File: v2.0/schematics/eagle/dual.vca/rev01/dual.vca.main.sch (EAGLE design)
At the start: 50 parts, among them IC1 TL084P, IC2 TL082P, IC3 LM324N, T1 BC547, T2 BC547, T3 BC547

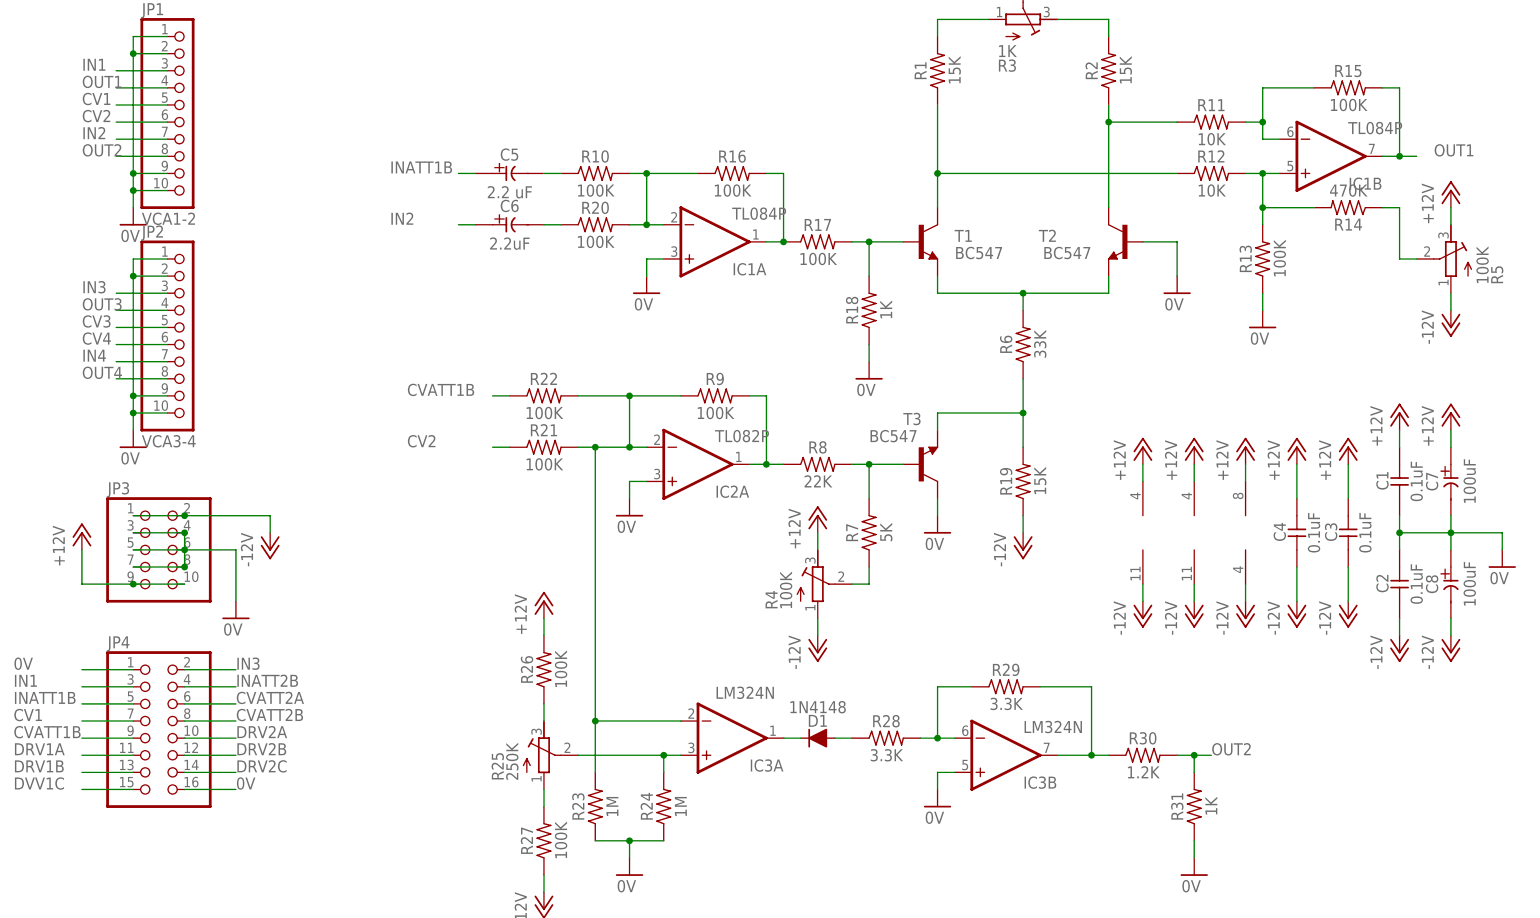
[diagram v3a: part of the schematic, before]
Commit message: Add DRV to dual.vca schem
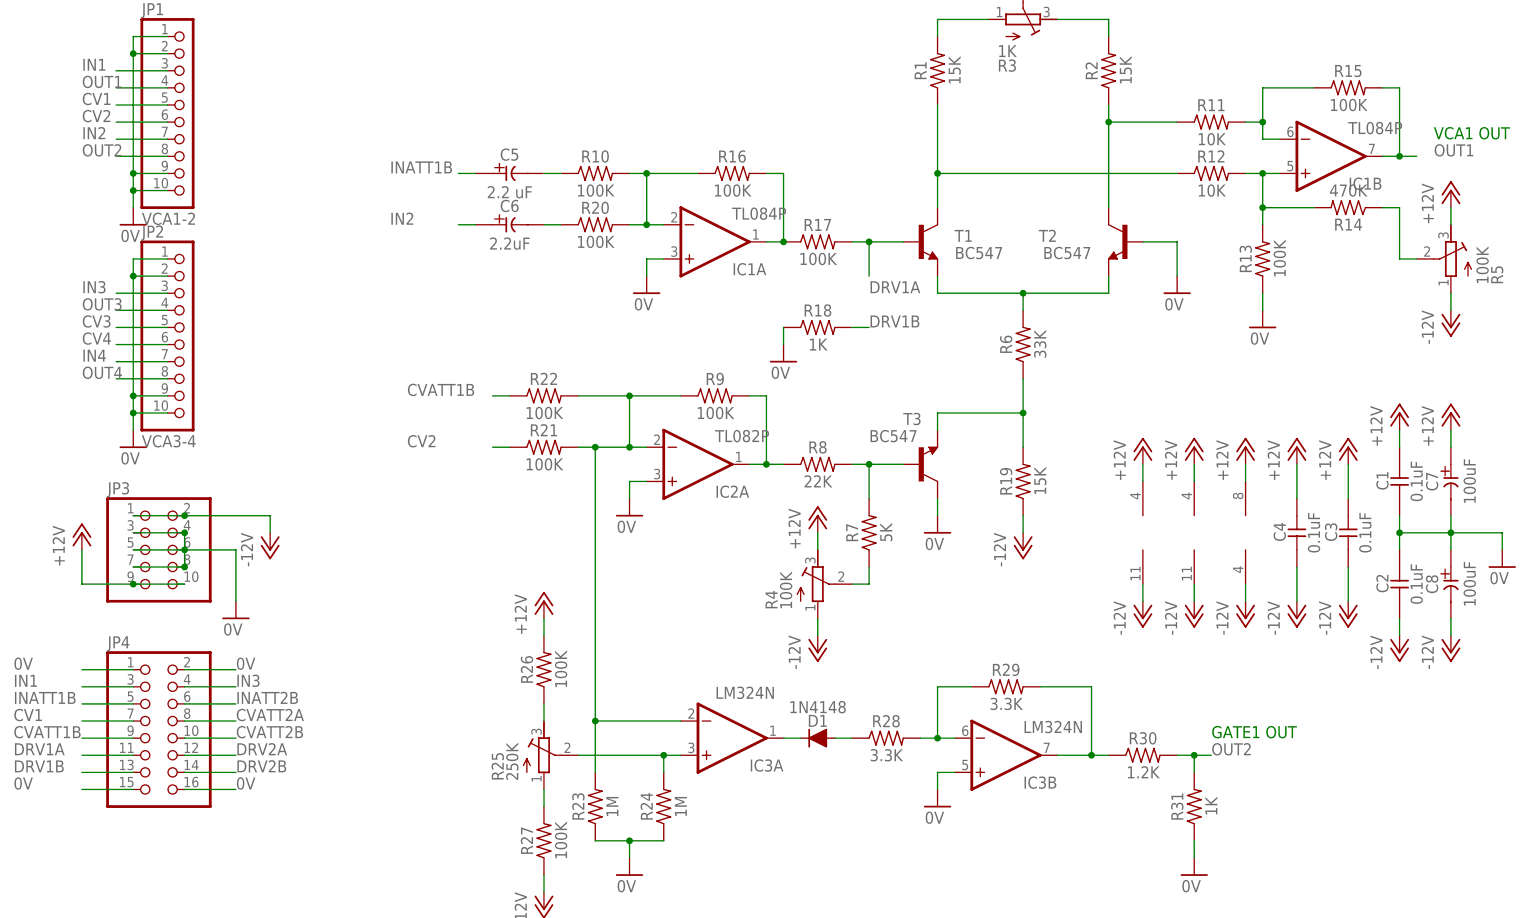
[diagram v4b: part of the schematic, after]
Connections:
- removed net DRV2C: JP4.14
- removed net DVV1C: JP4.15
- removed net N$4: R17.2, R18.2, T1.B
- net 0V: now also JP4.15, JP4.2
- net CVATT2A: now also JP4.8; no longer JP4.6
- net CVATT2B: now also JP4.10; no longer JP4.8
- net DRV1A: now also R17.2, T1.B
- net DRV1B: now also R18.2
- net DRV2A: now also JP4.12; no longer JP4.10
- net DRV2B: now also JP4.14; no longer JP4.12
- net IN3: now also JP4.4; no longer JP4.2
- net INATT2B: now also JP4.6; no longer JP4.4
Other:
- note added: "GATE1 OUT"
- note added: "VCA1 OUT"
- moved on the sheet: R18
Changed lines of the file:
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@@
 <plain>
 <text x="2.54" y="99.06" size="1.778" layer="91">VCA adapted from: https://yusynth.net/Modular/EN/VCA/index.html</text>
+<text x="127" y="-15.24" size="1.778" layer="91">GATE1 OUT</text>
+<text x="160.02" y="73.66" size="1.778" layer="91">VCA1 OUT</text>
 </plain>
 <instances>
@@
 <attribute name="VALUE" x="68.58" y="55.88" size="1.778" layer="96" align="center"/>
 </instance>
-<instance part="R18" gate="G$1" x="76.2" y="48.26" smashed="yes" rot="R90">
-<attribute name="NAME" x="73.6854" y="48.26" size="1.778" layer="95" rot="R90" align="center"/>
-<attribute name="VALUE" x="78.74" y="48.26" size="1.778" layer="96" rot="R90" align="center"/>
-</instance>
-<instance part="GND7" gate="1" x="76.2" y="38.1" smashed="yes">
-<attribute name="VALUE" x="74.295" y="35.56" size="1.778" layer="96"/>
+<instance part="R18" gate="G$1" x="68.58" y="45.72" smashed="yes">
+<attribute name="NAME" x="68.58" y="48.2346" size="1.778" layer="95" align="center"/>
+<attribute name="VALUE" x="68.58" y="43.18" size="1.778" layer="96" align="center"/>
+</instance>
+<instance part="GND7" gate="1" x="63.5" y="40.64" smashed="yes">
+<attribute name="VALUE" x="61.595" y="38.1" size="1.778" layer="96"/>
 </instance>
 <instance part="R19" gate="G$1" x="99.06" y="22.86" smashed="yes" rot="R90">
@@
 <pinref part="R18" gate="G$1" pin="1"/>
 <pinref part="GND7" gate="1" pin="0V"/>
-<wire x1="76.2" y1="43.18" x2="76.2" y2="40.64" width="0.1524" layer="91"/>
+<wire x1="63.5" y1="45.72" x2="63.5" y2="43.18" width="0.1524" layer="91"/>
 </segment>
 <segment>
@@
 <pinref part="GND11" gate="1" pin="0V"/>
 <wire x1="124.46" y1="-30.48" x2="124.46" y2="-33.02" width="0.1524" layer="91"/>
+</segment>
+<segment>
+<pinref part="JP4" gate="A" pin="15"/>
+<wire x1="-33.02" y1="-22.86" x2="-40.64" y2="-22.86" width="0.1524" layer="91"/>
+<label x="-50.8" y="-22.86" size="1.778" layer="95"/>
+</segment>
+<segment>
+<pinref part="JP4" gate="A" pin="2"/>
+<wire x1="-25.4" y1="-5.08" x2="-17.78" y2="-5.08" width="0.1524" layer="91"/>
+<label x="-17.78" y="-5.08" size="1.778" layer="95"/>
 </segment>
 </net>
@@
 </segment>
 <segment>
-<pinref part="JP4" gate="A" pin="2"/>
-<wire x1="-25.4" y1="-5.08" x2="-17.78" y2="-5.08" width="0.1524" layer="91"/>
-<label x="-17.78" y="-5.08" size="1.778" layer="95"/>
+<pinref part="JP4" gate="A" pin="4"/>
+<wire x1="-25.4" y1="-7.62" x2="-17.78" y2="-7.62" width="0.1524" layer="91"/>
+<label x="-17.78" y="-7.62" size="1.778" layer="95"/>
 </segment>
 </net>
@@
 <wire x1="60.96" y1="58.42" x2="63.5" y2="58.42" width="0.1524" layer="91"/>
 <junction x="63.5" y="58.42"/>
-</segment>
-</net>
-<net name="N$4" class="0">
-<segment>
-<pinref part="R17" gate="G$1" pin="2"/>
-<wire x1="73.66" y1="58.42" x2="76.2" y2="58.42" width="0.1524" layer="91"/>
-<pinref part="R18" gate="G$1" pin="2"/>
-<wire x1="76.2" y1="53.34" x2="76.2" y2="58.42" width="0.1524" layer="91"/>
-<pinref part="T1" gate="G$1" pin="B"/>
-<wire x1="76.2" y1="58.42" x2="81.28" y2="58.42" width="0.1524" layer="91"/>
-<junction x="76.2" y="58.42"/>
 </segment>
 </net>
@@
 <label x="-50.8" y="-17.78" size="1.778" layer="95"/>
 </segment>
+<segment>
+<pinref part="R17" gate="G$1" pin="2"/>
+<pinref part="T1" gate="G$1" pin="B"/>
+<wire x1="73.66" y1="58.42" x2="76.2" y2="58.42" width="0.1524" layer="91"/>
+<wire x1="76.2" y1="58.42" x2="81.28" y2="58.42" width="0.1524" layer="91"/>
+<wire x1="76.2" y1="58.42" x2="76.2" y2="53.34" width="0.1524" layer="91"/>
+<junction x="76.2" y="58.42"/>
+<label x="76.2" y="50.8" size="1.778" layer="95"/>
+</segment>
 </net>
 <net name="DRV1B" class="0">
@@
 <label x="-50.8" y="-20.32" size="1.778" layer="95"/>
 </segment>
-</net>
-<net name="DVV1C" class="0">
-<segment>
-<pinref part="JP4" gate="A" pin="15"/>
-<wire x1="-33.02" y1="-22.86" x2="-40.64" y2="-22.86" width="0.1524" layer="91"/>
-<label x="-50.8" y="-22.86" size="1.778" layer="95"/>
+<segment>
+<pinref part="R18" gate="G$1" pin="2"/>
+<wire x1="73.66" y1="45.72" x2="76.2" y2="45.72" width="0.1524" layer="91"/>
+<label x="76.2" y="45.72" size="1.778" layer="95"/>
 </segment>
 </net>
 <net name="INATT2B" class="0">
-<segment>
-<pinref part="JP4" gate="A" pin="4"/>
-<wire x1="-25.4" y1="-7.62" x2="-17.78" y2="-7.62" width="0.1524" layer="91"/>
-<label x="-17.78" y="-7.62" size="1.778" layer="95"/>
-</segment>
-</net>
-<net name="CVATT2A" class="0">
 <segment>
 <pinref part="JP4" gate="A" pin="6"/>
@@
 </segment>
 </net>
-<net name="CVATT2B" class="0">
+<net name="CVATT2A" class="0">
 <segment>
 <pinref part="JP4" gate="A" pin="8"/>
@@
 </segment>
 </net>
-<net name="DRV2A" class="0">
+<net name="CVATT2B" class="0">
 <segment>
 <pinref part="JP4" gate="A" pin="10"/>
@@
 </segment>
 </net>
-<net name="DRV2B" class="0">
+<net name="DRV2A" class="0">
 <segment>
 <pinref part="JP4" gate="A" pin="12"/>
@@
 </segment>
 </net>
-<net name="DRV2C" class="0">
+<net name="DRV2B" class="0">
 <segment>
 <pinref part="JP4" gate="A" pin="14"/>

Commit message: Iniital board layout for main dual.vca
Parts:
- removed JP3: (no value), pinhead:PINHD-2X5
- removed JP4: (no value), pinhead:PINHD-2X8
- added C10: 2.2uF, _common:CE-USE2-5
- added C11: 0.1uF, _common:CC-US025-024X044
- added C9: 2.2 uF, _common:CE-USE2-5
- added CV1ATT, CV3ATT: 250K LIN, _common:3RP/1610N
- added D2: 1N4148, _common:1N4148
- added DRV1, DRV2: 10K LIN, _common:3RP/1610N
- added IN1ATT, IN3ATT: 250K LOG, _common:3RP/1610N
- added R32, R33, R34, R36, R37, R38, R41, R42, R43, R59, R60: 100K, _common:R
- added R35: 250K, rcl:R-TRIMM3339P
- added R39, R40: 1M, _common:R
- added R44, R56: 1K, _common:R
- added R45: 22K, _common:R
- added R46, R62: 100K, rcl:R-TRIMM3339P
- added R47: 5K, _common:R
- added R48, R50: 3.3K, _common:R
- added R49, R53, R54: 15K, _common:R
- added R51: 1K, rcl:R-TRIMM3339P
- added R52: 33K, _common:R
- added R55: 1.2K, _common:R
- added R57, R58: 10K, _common:R
- added R61: 470K, _common:R
- added T4, T5, T6: BC547, transistor:BC547
- C5: value 2.2 uF -> 100uF; device _common:CE-USE2-5 -> _common:CE-USE5-8.5
- C6: value 2.2uF -> 100uF; device _common:CE-USE2-5 -> _common:CE-USE5-8.5
- C7: value 100uF -> 2.2 uF
- C8: value 100uF -> 2.2uF
- IC1: value TL084P -> TL082P; device linear:TL084P -> linear:TL082P
- IC2: value TL082P -> TL084P; device linear:TL082P -> linear:TL084P
- JP1: value VCA1-2 -> (none); device pinhead:PINHD-1X10 -> pinhead:PINHD-2X5
- JP2: value VCA3-4 -> (none); device pinhead:PINHD-1X10 -> pinhead:PINHD-2X8
- R1, R2: value 15K -> 100K
- R11, R12: value 10K -> 100K
- R13: value 100K -> 1K
- R14: value 470K -> 22K
- R15: device _common:R -> rcl:R-TRIMM3339P
- R16: value 100K -> 5K
- R17: value 100K -> 3.3K
- R18: value 1K -> 15K
- R19: value 15K -> 3.3K
- R20: value 100K -> 1K; device _common:R -> rcl:R-TRIMM3339P
- R21: value 100K -> 33K
- R22: value 100K -> 15K
- R23: value 1M -> 15K
- R24: value 1M -> 1.2K
- R25: value 250K -> 1K; device rcl:R-TRIMM3339P -> _common:R
- R26, R27: value 100K -> 10K
- R28, R29: value 3.3K -> 100K
- R3: value 1K -> 100K; device rcl:R-TRIMM3339P -> _common:R
- R30: value 1.2K -> 470K
- R31: value 1K -> 100K; device _common:R -> rcl:R-TRIMM3339P
- R4: value 100K -> 250K
- R5: device rcl:R-TRIMM3339P -> _common:R
- R6: value 33K -> 100K
- R7: value 5K -> 100K
- R8: value 22K -> 1M
- R9: value 100K -> 1M
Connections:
- removed net CVATT1B: JP4.9, R22.1
- removed net CVATT2A: JP4.8
- removed net CVATT2B: JP4.10
- removed net DRV1A: JP4.11, R17.2, T1.B
- removed net DRV1B: JP4.13, R18.2
- removed net DRV2A: JP4.12
- removed net DRV2B: JP4.14
- removed net INATT1B: C5.+, JP4.5
- removed net INATT2B: JP4.6
- new net N$26: DRV2.E, DRV2.S, R44.2
- new net N$27: C7.+, IN1ATT.S
- new net N$28: IC2A.-IN, R37.2, R38.2, R42.1
- new net N$29: CV1ATT.S, R1.1
- new net N$30: IC2A.OUT, R42.2, R43.1
- new net N$31: R49.1, R58.1, T4.C
- new net N$32: R49.2, R51.A
- new net N$33: R51.E, R54.2
- new net N$34: R54.1, R57.1, T6.C
- new net N$35: R52.2, T4.E, T6.E
- new net N$36: IC2B.-IN, R57.2, R60.1
- new net N$37: IC2B.+IN, R58.2, R59.2, R61.2
- new net N$38: R61.1, R62.S
- new net N$39: R52.1, R53.2, T5.E
- new net N$4: DRV1.A, R12.2, T1.B
- new net N$40: R45.2, R47.2, T5.B
- new net N$41: R46.S, R47.1
- new net N$42: IC1A.OUT, R41.2, R45.1
- new net N$43: IC1A.-IN, IC3A.-IN, R32.2, R33.2, R39.2, R41.1
- new net N$44: C9.-, R37.1
- new net N$45: C10.-, R38.1
- new net N$46: IC3A.+IN, R35.S, R40.2
- new net N$47: R34.1, R35.E
- new net N$48: R35.A, R36.2
- new net N$49: D2.C, IC3A.OUT
- new net N$50: D2.A, R48.1
- new net N$51: IC3B.-IN, R48.2, R50.1
- new net N$52: IC3B.OUT, R50.2, R55.1
- new net N$53: DRV2.A, R43.2, T4.B
- new net N$54: DRV1.E, DRV1.S, R13.2
- new net N$55: C9.+, IN3ATT.S
- new net N$56: CV3ATT.S, R32.1
- net +12V: now also C11.1, C2.1, C5.+, JP1.10, JP1.9, R15.E, R20.S, R3.2, R31.E, R34.2, R46.E, R51.S, R62.E; no longer C4.1, C7.+, JP3.10, JP3.9, R26.2, R3.S, R4.E, R5.E
- net -12V: now also C1.2, C11.2, C6.-, JP1.1, JP1.2, R15.A, R22.1, R31.A, R36.1, R46.A, R5.1, R53.1, R62.A; no longer C3.2, C8.-, JP3.1, JP3.2, R19.1, R27.1, R4.A, R5.A
- net 0V: now also C3.2, C4.1, C5.-, C6.+, CV1ATT.A, CV3ATT.A, IC1B.+IN, IC2D.+IN, IC3C.+IN, IN1ATT.A, IN3ATT.A, JP1.3, JP1.4, JP1.5, JP1.6, JP1.7, JP1.8, JP2.15, JP2.16, R25.1, R28.1, R39.1, R40.1, R44.1, R56.1, R59.1, R8.1, R9.1, T2.C, T3.B, T5.C, T6.B; no longer C1.2, C2.1, C7.-, C8.+, JP1.1, JP1.10, JP1.2, JP1.9, JP2.10, JP2.9, JP3.3, JP3.4, JP3.5, JP3.6, JP3.7, JP3.8, JP4.1, JP4.15, JP4.16, JP4.2, R18.1, R23.1, R24.1, R31.1, T2.B, T3.C
- net CV1: now also CV1ATT.E, JP2.7; no longer JP1.5, JP4.7
- net CV2: now also JP2.9, R2.1; no longer JP1.6, R21.1
- net CV3: now also CV3ATT.E, JP2.8; no longer JP2.5
- net CV4: now also JP2.10, R33.1; no longer JP2.6
- net IN1: now also IN1ATT.E, JP2.3; no longer JP1.3, JP4.3
- net IN2: now also C8.+, JP2.11; no longer C6.+, JP1.7
- net IN3: now also IN3ATT.E, JP2.4; no longer JP2.3, JP4.4
- net IN4: now also C10.+, JP2.12; no longer JP2.7
- net N$1: now also IC2D.-IN, R11.1, R6.2, R7.2; no longer IC1A.-IN, R10.2, R16.1, R20.2
- net N$10: now also R30.1, R31.S; no longer R14.1, R5.S
- net N$11: now also C7.-, R6.1; no longer C5.-, R10.1
- net N$12: now also IC2C.+IN, R27.2, R28.2, R30.2; no longer IC1B.+IN, R12.2, R13.2, R14.2
- net N$13: now also R21.1, R22.2, T2.E; no longer R19.2, R6.1, T3.E
- net N$14: now also C8.-, R7.1; no longer C6.-, R20.1
- net N$15: now also R14.2, R16.2, T2.B; no longer R7.2, R8.2, T3.B
- net N$16: now also R15.S, R16.1; no longer R4.S, R7.1
- net N$17: now also IC1B.OUT, R10.2, R14.1; no longer IC2A.OUT, R8.1, R9.2
- net N$18: now also IC3D.+IN, R4.S, R9.2; no longer IC3A.+IN, R24.2, R25.S
- net N$19: now also IC1B.-IN, IC3D.-IN, R1.2, R10.1, R2.2, R8.2; no longer IC2A.-IN, IC3A.-IN, R21.2, R22.2, R23.2, R9.1
- net N$2: now also IC2C.-IN, R26.2, R29.1; no longer IC1B.-IN, R11.2, R15.1
- net N$20: now also R3.1, R4.E; no longer R25.E, R26.1
- net N$21: now also R4.A, R5.2; no longer R25.A, R27.2
- net N$22: now also IC3D.OUT; no longer IC3A.OUT
- net N$23: now also R17.1; no longer R28.1
- net N$24: now also IC3C.-IN, R17.2, R19.1; no longer IC3B.-IN, R28.2, R29.1
- net N$25: now also IC3C.OUT, R19.2, R24.1; no longer IC3B.OUT, R29.2, R30.1
- net N$3: now also IC2D.OUT, R11.2, R12.1; no longer IC1A.OUT, R16.2, R17.1
- net N$5: now also R18.1, R27.1; no longer R1.1, R12.1
- net N$6: now also R18.2, R20.A; no longer R1.2, R3.A
- net N$7: now also R20.E, R23.2; no longer R2.2, R3.E
- net N$8: now also R23.1, R26.1, T3.C; no longer R11.1, R2.1, T2.C
- net N$9: now also R21.2, T3.E; no longer R6.2, T2.E
- net OUT1: now also IC2C.OUT, JP2.5, R29.2; no longer IC1B.OUT, JP1.4, R15.2
- net OUT2: now also JP2.13, R24.2, R25.2; no longer JP1.8, R30.2, R31.2
- net OUT3: now also IC2B.OUT, JP2.6, R60.2; no longer JP2.4
- net OUT4: now also JP2.14, R55.2, R56.2; no longer JP2.8
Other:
- moved on the sheet: C1, C2, C3, C4, C5, C6, C7, C8, IC1A, IC1B, IC2A, IC3A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

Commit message: Added generic prototype board with autoroute and ground plane
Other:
- note added: "Dual VCA - Rev 01 - Nov 2021"
- moved on the sheet: C1, C10, C11, C2, C3, C4, C5, C6, C9, CV3ATT, D2, DRV2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

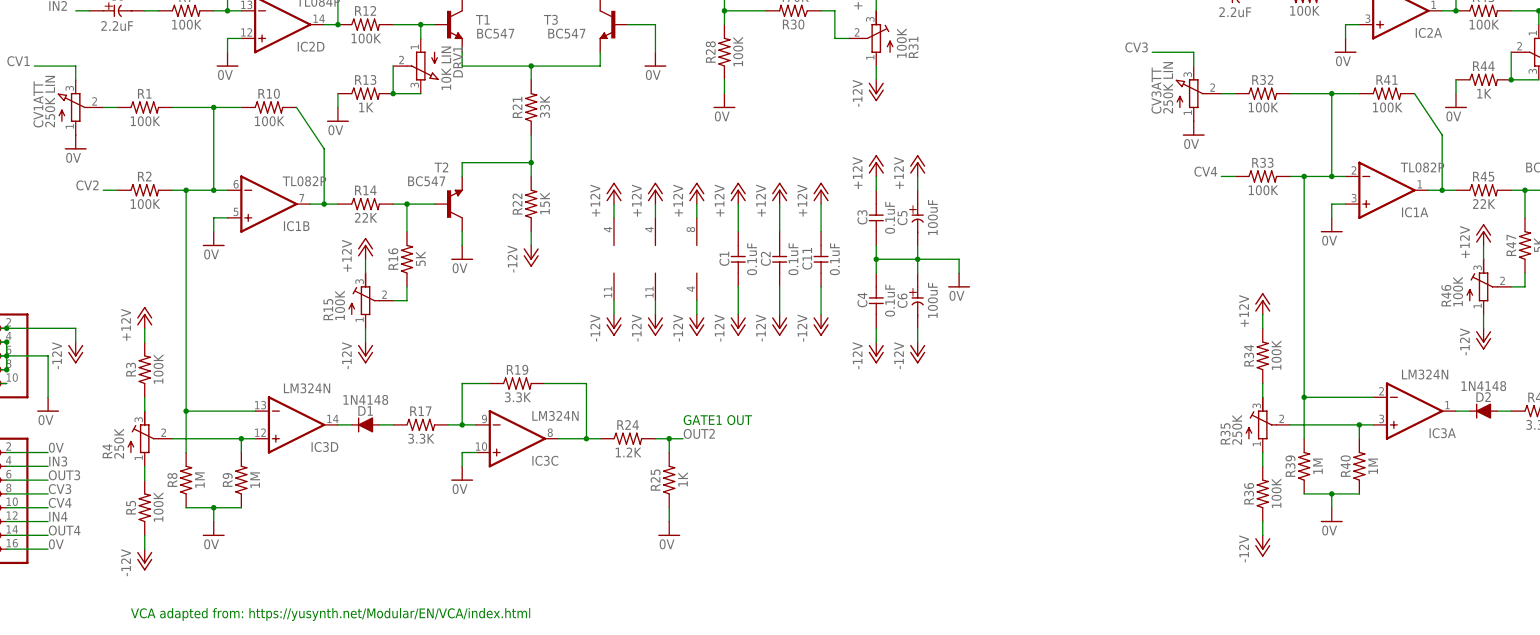
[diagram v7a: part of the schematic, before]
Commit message: Adjusted Dual.Seq comparrator
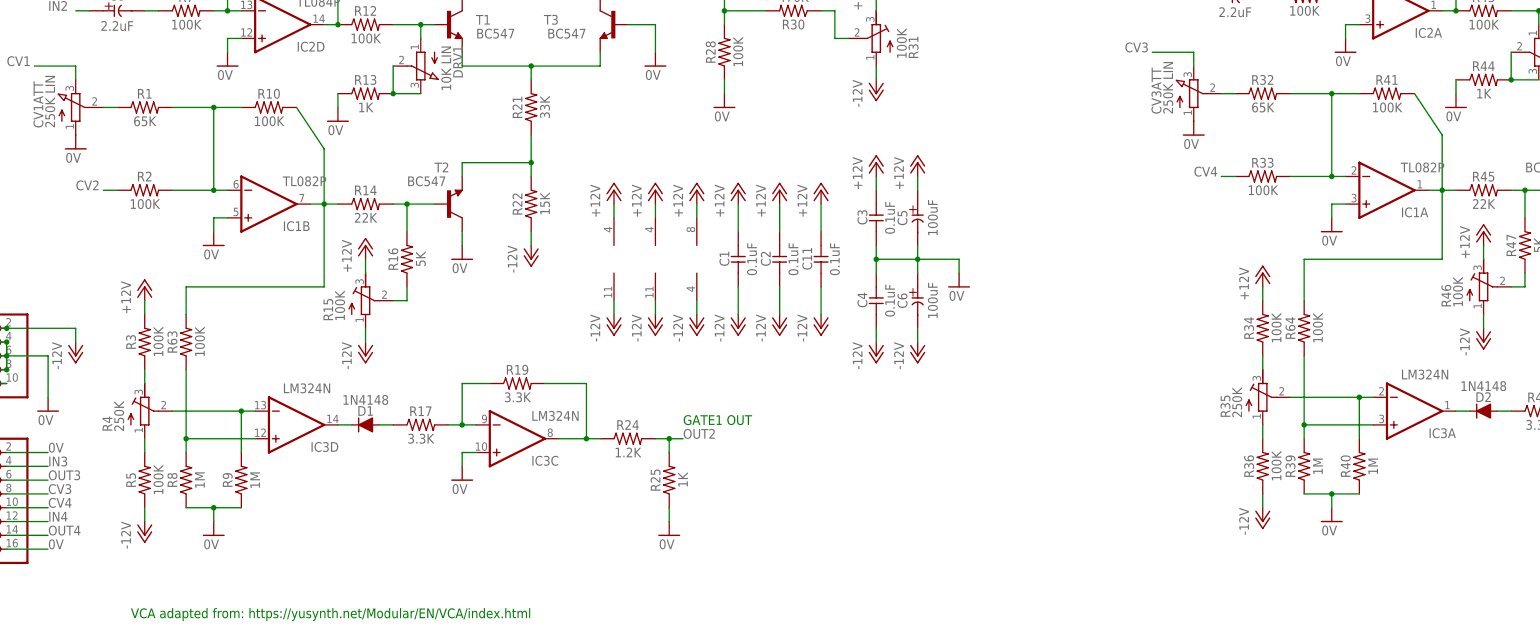
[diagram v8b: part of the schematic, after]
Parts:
- added R63, R64: 100K, _common:R
- R1, R32: value 100K -> 65K
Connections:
- new net N$57: IC3D.+IN, R63.1, R8.2
- new net N$58: IC3A.-IN, R35.S, R40.2
- net N$17: now also R63.2
- net N$18: now also IC3D.-IN; no longer IC3D.+IN
- net N$19: no longer IC3D.-IN, R8.2
- net N$42: now also R64.2
- net N$43: no longer IC3A.-IN, R39.2
- net N$46: now also R39.2, R64.1; no longer R35.S, R40.2
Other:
- moved on the sheet: R3, R34, R35, R36, R4, R5
